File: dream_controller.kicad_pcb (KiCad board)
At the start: 2 copper layers, 37 parts, among them J1 USB_B_Micro, J2 Conn_01x04_Male, Q1 Q_NMOS_DGS, Q2 Q_NMOS_DGS, Q3 Q_NMOS_DGS, Q4 Q_NMOS_DGS, U1 RP2040, U2 W25Q32JVSS, U3 MAX4073TAUT, U4 DRV8770RGER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

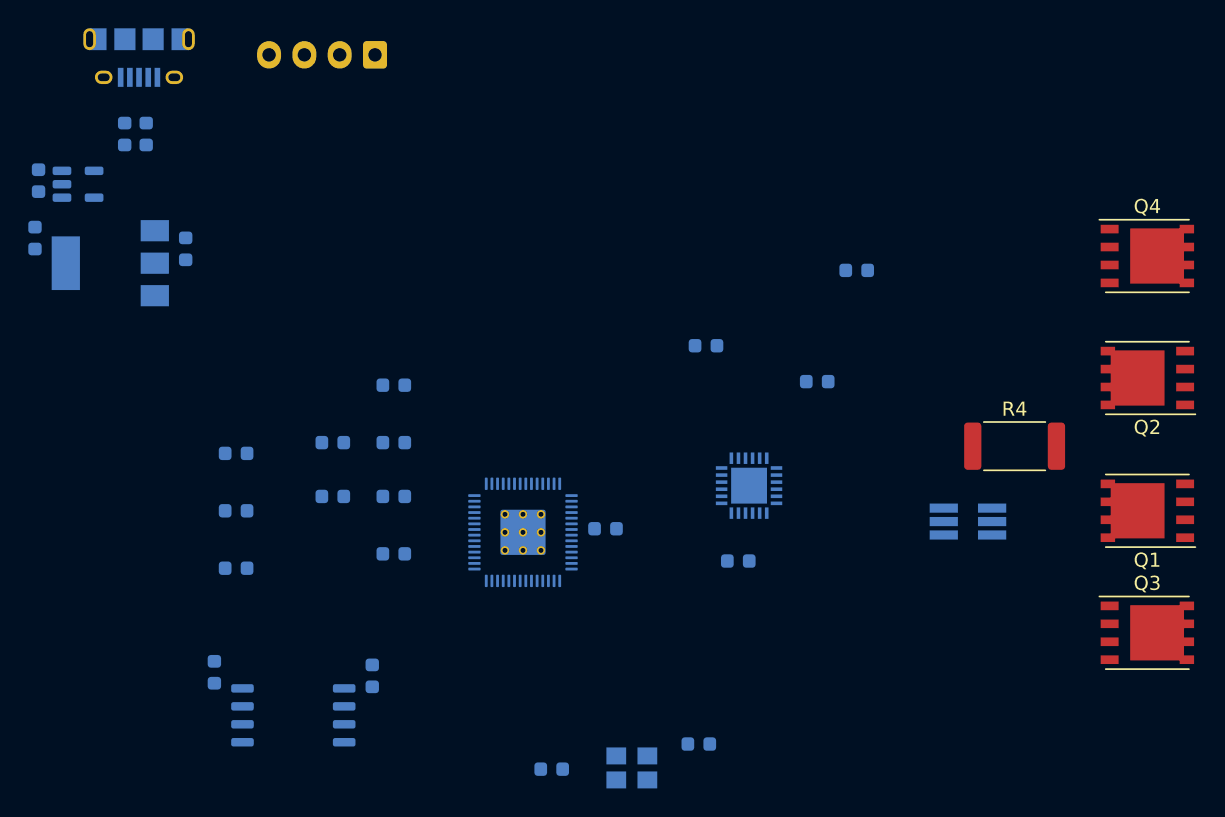
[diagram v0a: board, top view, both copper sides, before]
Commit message: updating to CAN
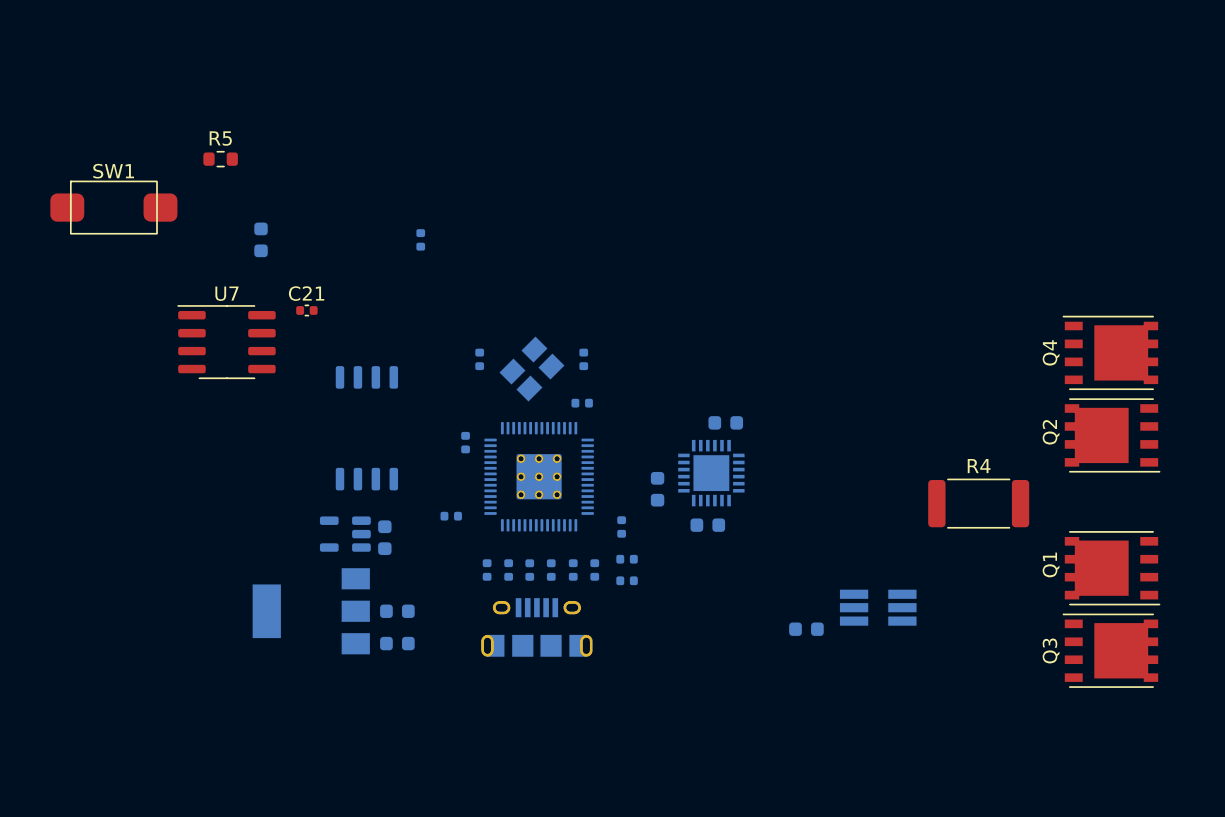
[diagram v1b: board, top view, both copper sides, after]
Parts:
- removed J2: Conn_01x04_Male, Connector_JST:JST_XH_B4B-XH-A_1x04_P2.50mm_Vertical
- added C21: 100n, Capacitor_SMD:C_0402_1005Metric, F.Cu at (113.2, 105.5)
- added R5: 1k, Resistor_SMD:R_0603_1608Metric, F.Cu at (107.1, 94.7)
- added SW1: SW_Push, RP2040:PTS636, F.Cu at (99.6, 98.2)
- added U7: MAX3051, Package_SO:SOIC-8_3.9x4.9mm_P1.27mm, F.Cu at (107.6, 107.7)
- C10, C11, C12, C13, C14, C15, C4, C5, C6, C7, C8, C9, R1, R2, R3: footprint Capacitor_SMD:C_0603_1608Metric -> Capacitor_SMD:C_0402_1005Metric
- moved J1 49.2 mm to (129.5, 127.9), turned to 180 degrees
- moved R2 43.2 mm to (130.5, 123.8), turned to 90 degrees
- moved R1 41.1 mm to (129.0, 123.8), turned to -90 degrees
- moved C3 38.5 mm to (119.6, 129.0), turned to 0 degrees
- moved C2 35.2 mm to (118.7, 121.5), turned to -90 degrees
- moved C15 31.3 mm to (125.5, 108.9), turned to -90 degrees
- moved U6 31.2 mm to (116.0, 121.3), turned to 180 degrees
- moved R3 31.1 mm to (121.3, 100.5)
- moved C1 30.8 mm to (110.0, 100.5)
- moved C17 29.7 mm to (119.6, 126.7), turned to 0 degrees
- moved Y1 29.1 mm to (129.2, 109.6), turned to 45 degrees
- moved C14 29.1 mm to (132.8, 108.9), turned to -90 degrees
- moved U5 28.4 mm to (113.5, 126.7)
- moved C13 27.1 mm to (132.7, 112.0), turned to 0 degrees
- moved C12 24.2 mm to (132.1, 123.8), turned to -90 degrees
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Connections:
- U1 pad 18: unconnected-(U1-Pad18) -> /CAN_RX
- U1 pad 2: /SPI_MOSI -> unconnected-(U1-Pad2)
- U1 pad 24: unconnected-(U1-Pad24) -> /SWCLK
- U1 pad 25: unconnected-(U1-Pad25) -> /SWD
- U1 pad 27: unconnected-(U1-Pad27) -> /CAN_TX
- U1 pad 3: /SPI_CS -> unconnected-(U1-Pad3)
- U1 pad 34: /INHA -> /INLB
- U1 pad 35: /INHB -> /INLA
- U1 pad 36: /INLA -> /INHB
- U1 pad 37: /INLB -> /INHA
- U1 pad 4: /SPI_CLK -> unconnected-(U1-Pad4)
- U1 pad 5: /SPI_MISO -> unconnected-(U1-Pad5)
